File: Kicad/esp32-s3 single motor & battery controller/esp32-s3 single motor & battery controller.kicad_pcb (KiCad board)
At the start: 4 copper layers, 38.8 x 40.3 mm, 92 parts, among them J1 JST SH SM04B, J2 7 pin FPC 0.3mm, J3 Molex_PicoBlade_53048-0310 Ho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, Q3 PMOS,Si7157DP, Q4 PMOS, SW1 SW_Push, SW2 SW_Push, U1 AP2112K-3.3, U2 DRV8311HRRWR, U4 BQ25060, U5 ESP32-S3, U6 74HC595, Y1 40mhz, 10ppm

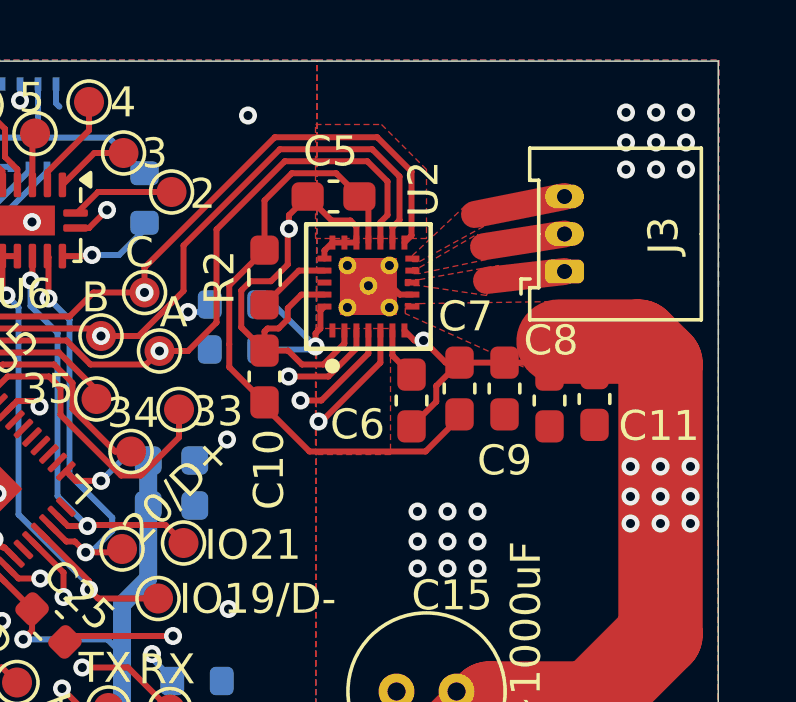
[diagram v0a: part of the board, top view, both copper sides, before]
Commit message: Started migrating driver to the back of the motor
If successful, this will save a ton of space. This will be a mess for awhile.
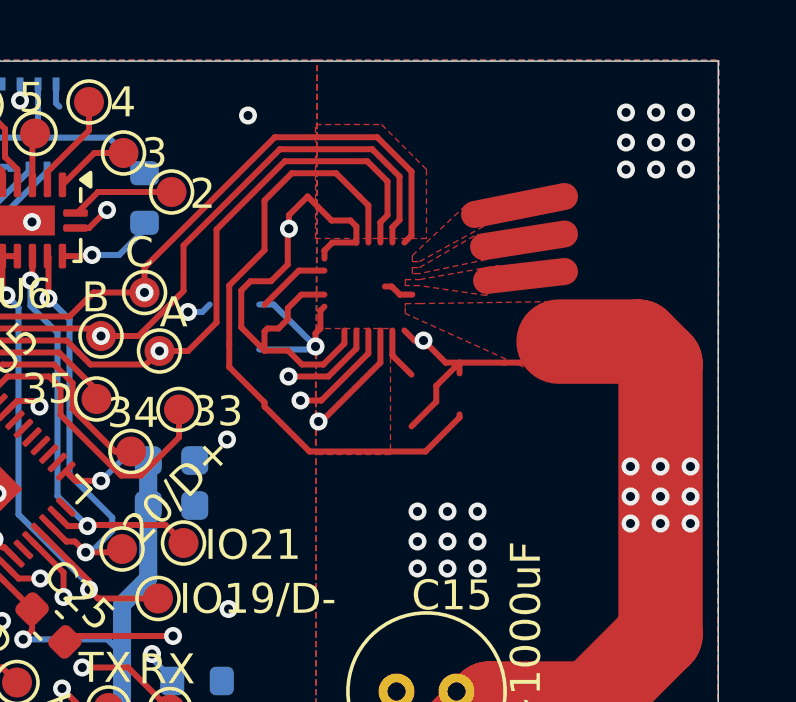
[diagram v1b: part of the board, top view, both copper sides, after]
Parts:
- removed C10: 0.1uF, Capacitor_SMD:C_0603_1608Metric_Pad1.08x0.95mm_HandSolder
- removed C11, C8: 22uF, Capacitor_SMD:C_0603_1608Metric_Pad1.08x0.95mm_HandSolder
- removed C5: 4.7uF, Capacitor_SMD:C_0603_1608Metric_Pad1.08x0.95mm_HandSolder
- removed C6, C7, C9: 0.1uF, 16v, Capacitor_SMD:C_0603_1608Metric_Pad1.08x0.95mm_HandSolder
- removed J3: Molex_PicoBlade_53048-0310 Horizontal 3P, Connector_Molex:Molex_PicoBlade_53048-0310_1x03_P1.25mm_Horizontal
- removed R1: 100k, Resistor_SMD:R_0603_1608Metric
- removed R2: 47k, Resistor_SMD:R_0603_1608Metric_Pad0.98x0.95mm_HandSolder
- removed R9: 150k, Resistor_SMD:R_0603_1608Metric
- removed U2: DRV8311HRRWR, custom_Driver_Motor:DRV8311_0.3mmVias
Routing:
- net (no net): track 0.00 -> 27.8 mm, vias 0 -> 2
- net /DRV8311/RegulatorOut: track 17.7 -> 0.00 mm, vias 1 -> 0
- net Net-(U2-SLEEP_N): track 5.82 -> 0.00 mm, vias 1 -> 0
- net Net-(U2-GAIN): track 2.47 -> 0.00 mm
- net Net-(U2-CP): track 1.74 -> 0.00 mm
- added copper zone on F.Cu, net (none)
- removed copper zone on F.Cu, net Net-(J3-Pin_1)
- removed copper zone on F.Cu, net Net-(J3-Pin_2)
- removed copper zone on F.Cu, net Net-(J3-Pin_3)

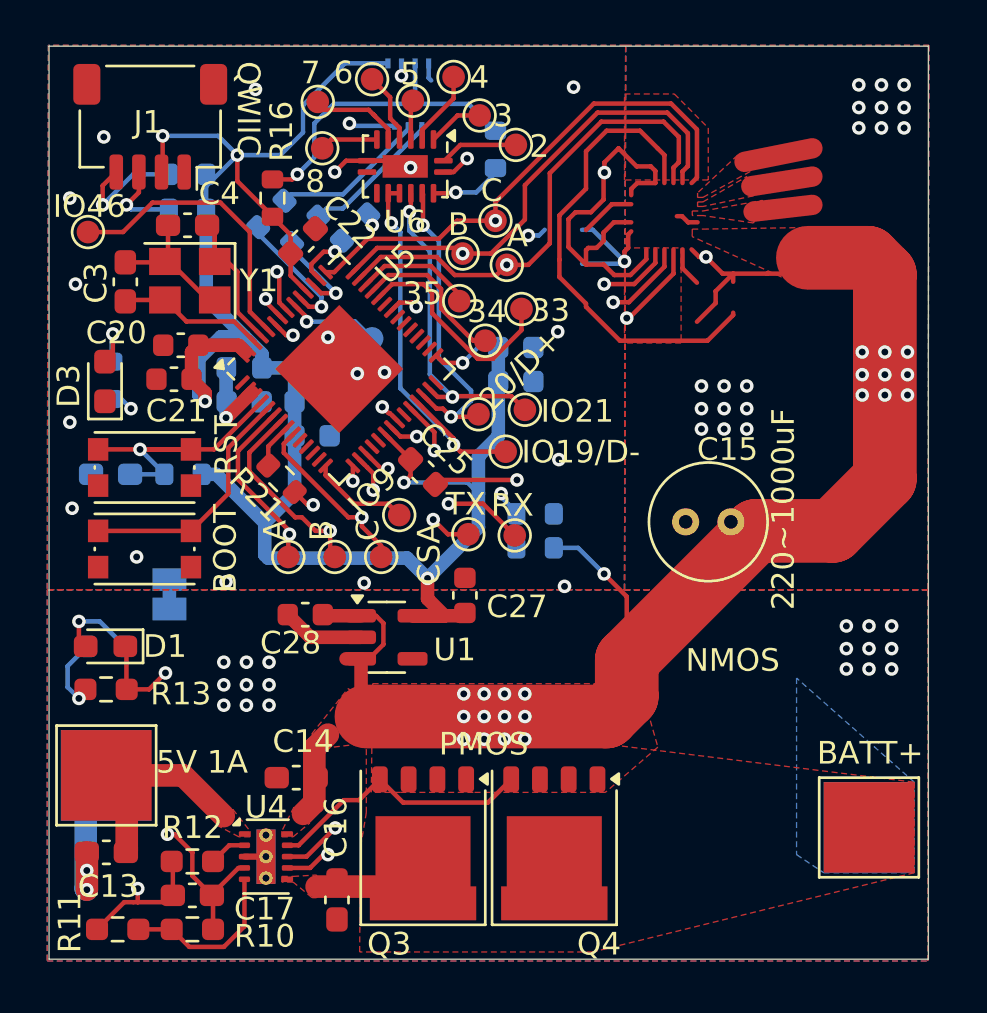
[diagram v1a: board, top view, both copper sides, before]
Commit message: Removed drv8311 section on the main board
Don't need it now that I have it off-board.
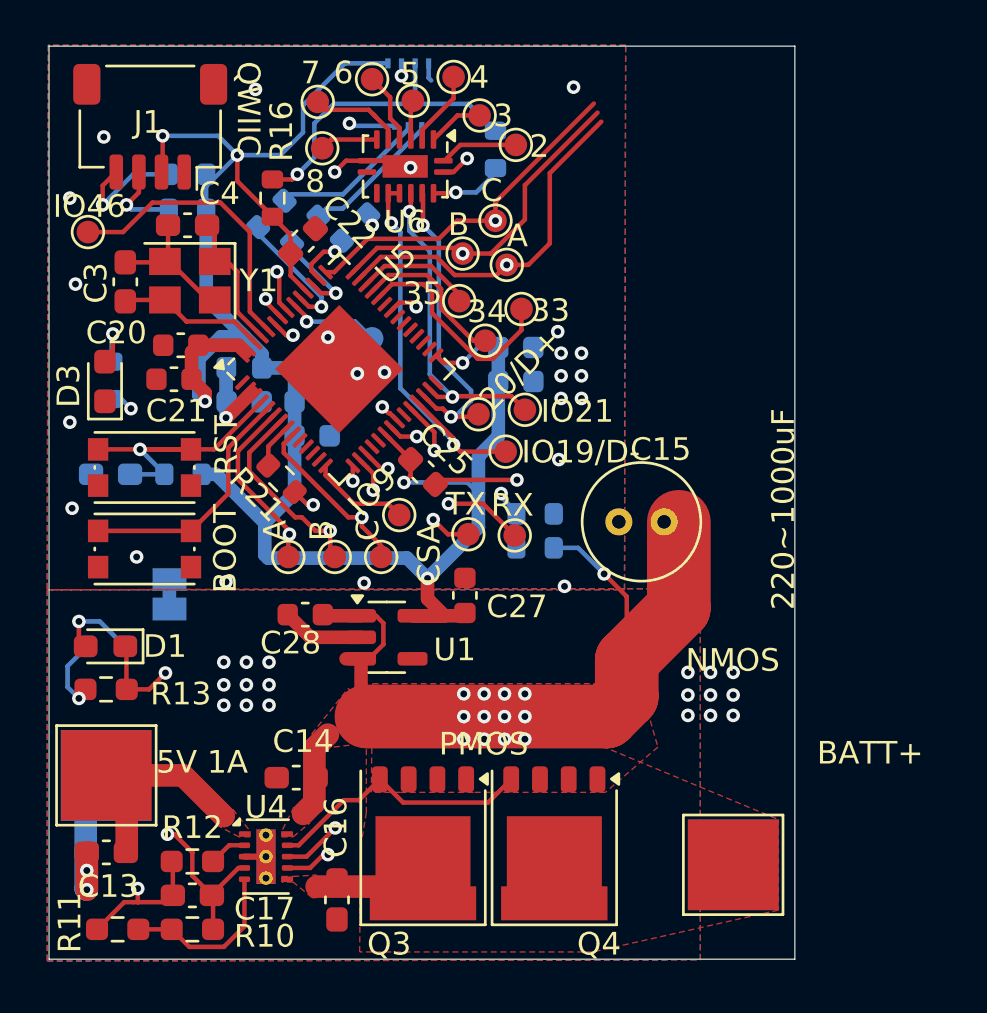
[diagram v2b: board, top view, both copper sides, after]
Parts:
- moved H1 6.22 mm to (152.9, 126.0)
- moved H2 6.22 mm to (152.9, 126.0)
- moved C15 2.95 mm to (149.8, 110.9)
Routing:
- net /MOTORPWR: track 114.5 -> 60.2 mm, vias 24 -> 13
- net (no net): track 27.8 -> 0.00 mm, vias 2 -> 0
- net GND: track 72.7 -> 51.6 mm
- net /1C: track 30.4 -> 22.9 mm
- net /1B: track 30.8 -> 24.2 mm
- net /1A: track 32.4 -> 26.6 mm
- net /1CSA-A: track 36.9 -> 33.0 mm, vias 2 -> 1
- net /1CSA-B: track 35.8 -> 32.1 mm, vias 2 -> 1
- net /1CSA-C: track 32.2 -> 28.9 mm, vias 2 -> 1
- net GNDPWR: track 12.7 -> 11.7 mm, vias 38 -> 26
- removed copper zone on F.Cu, net (none)
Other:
- board size 38.8 x 40.3 mm -> 32.9 x 40.3 mm

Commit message: Mostly finished Mainboard, adding silkscreen to magnetic encoder
I added pin headers to support my external driver board, and shrunk the whole design
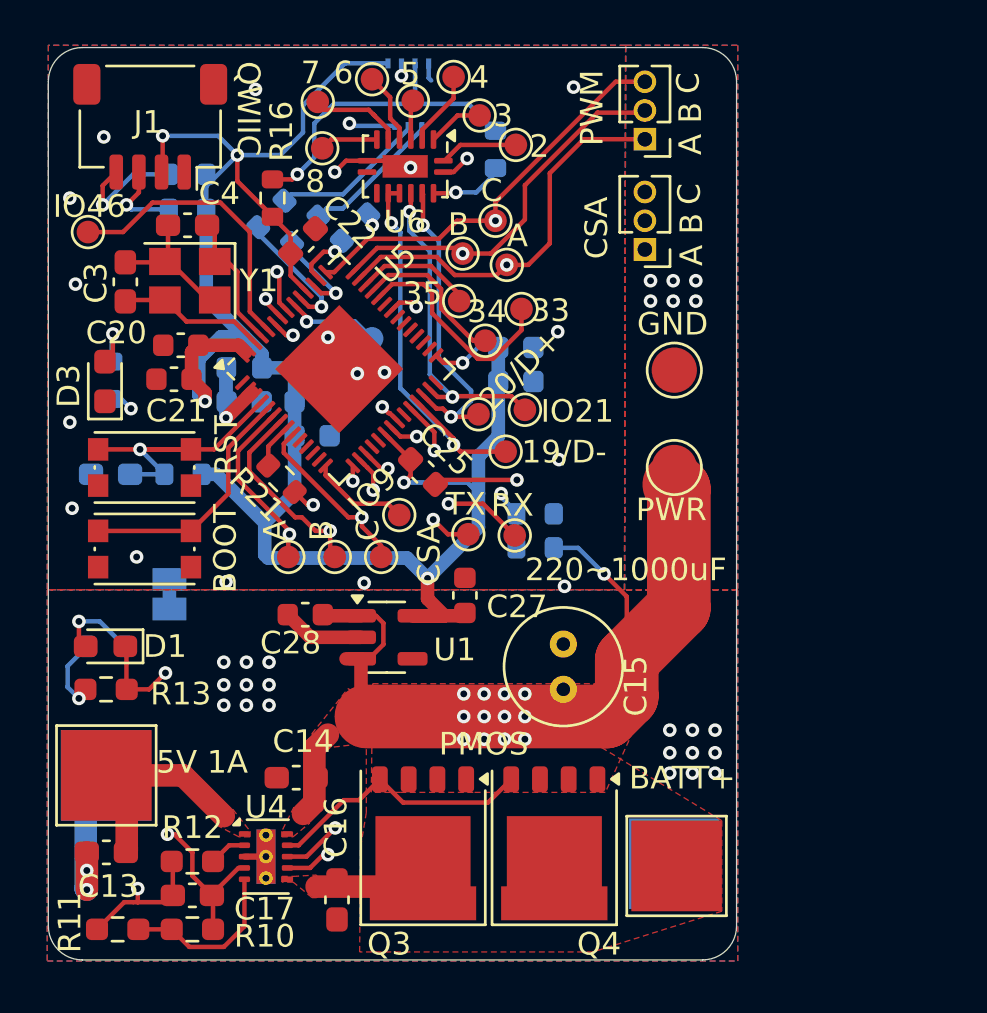
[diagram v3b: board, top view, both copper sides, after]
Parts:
- added H5: GND, TestPoint:TestPoint_Pad_D2.0mm, F.Cu at (150.3, 104.2)
- added H6: Power, TestPoint:TestPoint_Pad_D2.0mm, F.Cu at (150.3, 108.5)
- added J3: Conn_01x03, Connector_PinHeader_1.27mm:PinHeader_1x03_P1.27mm_Vertical, F.Cu at (149.0, 94.0)
- added J4: Conn_01x03, Connector_PinHeader_1.27mm:PinHeader_1x03_P1.27mm_Vertical, F.Cu at (149.0, 98.9)
- moved C15 8.63 mm to (145.4, 118.3), turned to 90 degrees
- moved H2 2.60 mm to (150.3, 126.0)
- moved H1 2.50 mm to (150.4, 126.1)
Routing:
- net /MOTORPWR: track 60.2 -> 41.5 mm
- net /1CSA-C: track 28.9 -> 33.3 mm
- net /1CSA-B: track 32.1 -> 35.7 mm
- net /1CSA-A: track 33.0 -> 36.1 mm
- net /1C: track 22.9 -> 25.6 mm
- net /1B: track 24.2 -> 26.3 mm
- net /1A: track 26.6 -> 28.2 mm
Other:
- board size 32.9 x 40.3 mm -> 30.4 x 40.3 mm
- board text added: "19/D-"
- board text added: "Encoder"
- board text added: "PWM"
- board text added: "PWR"
- board text added: "|||||||"
- board text added: "© 2024 Asher Edwards"
- board text removed: "Contacts facing PCB"
- board text removed: "Encoder FPC"
- board text removed: "IO19/D-"
- board text removed: "NMOS"
- board text removed: "© 2024 Asher James Edwards"

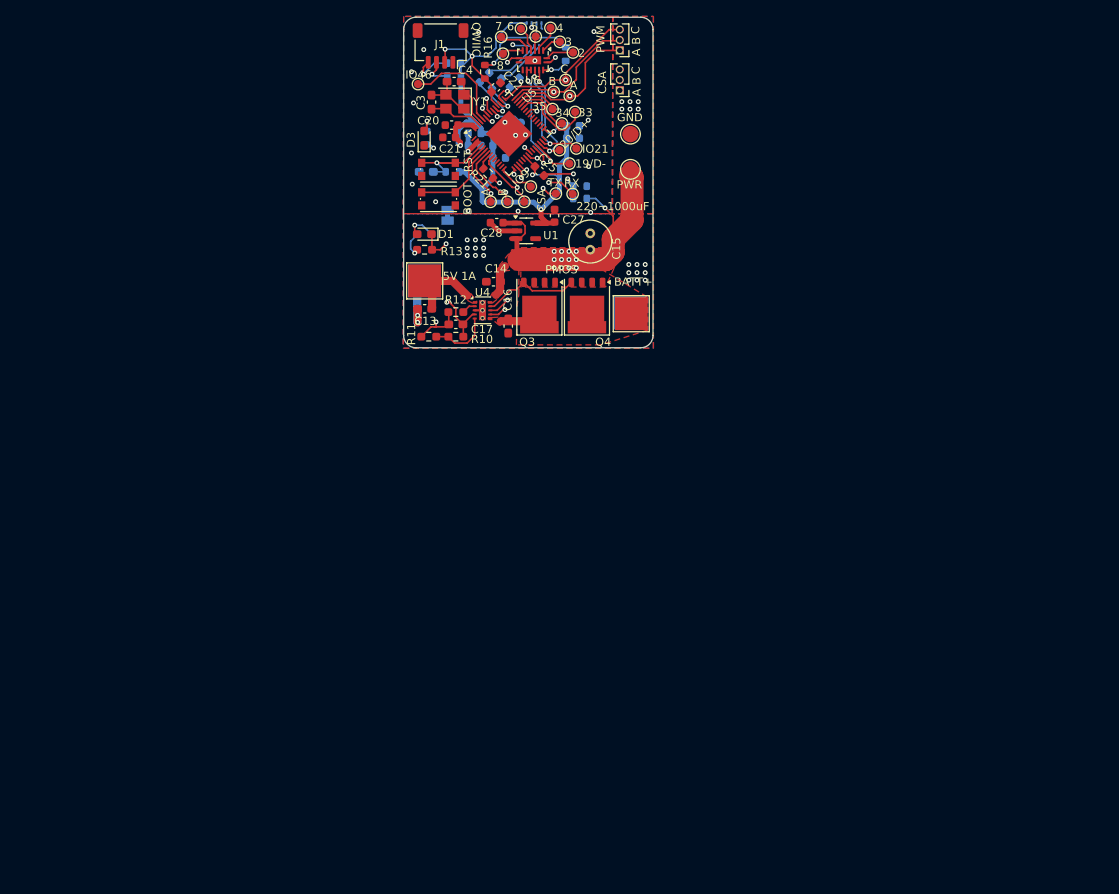
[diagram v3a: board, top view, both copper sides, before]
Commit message: Added footprints and started layout
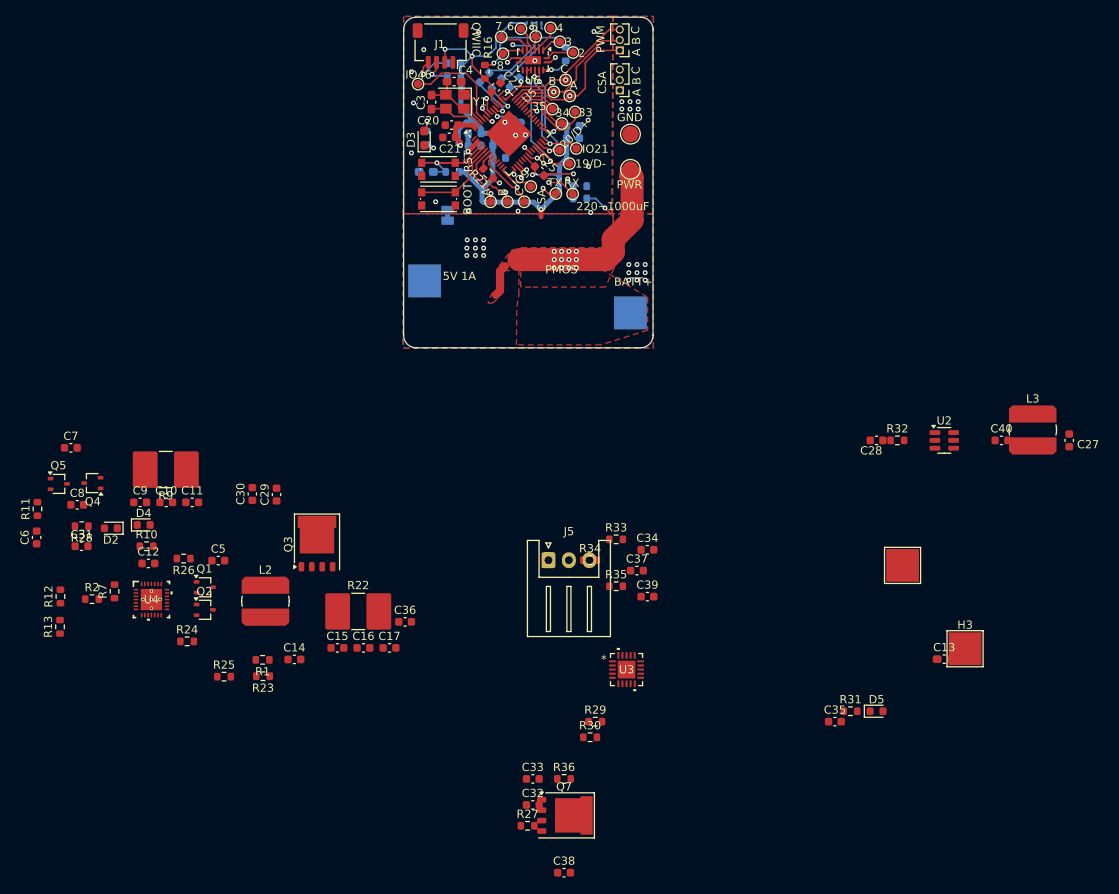
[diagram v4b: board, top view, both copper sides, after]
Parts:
- removed D1: Osram LT Q99G.01 green led, LED_SMD:LED_0603_1608Metric_Pad1.05x0.95mm_HandSolder
- removed R8: 402 ohm, Resistor_SMD:R_0603_1608Metric
- removed U1: AP2112K-3.3, Package_TO_SOT_SMD:SOT-23-5
- added C10: 0.1uF, Capacitor_SMD:C_0603_1608Metric, F.Cu at (93.7, 149.1)
- added C11: 0.01uF, Capacitor_SMD:C_0603_1608Metric, F.Cu at (96.9, 149.1)
- added C12: 1uf, Capacitor_SMD:C_0603_1608Metric, F.Cu at (91.5, 156.6)
- added C29: 10uF, Capacitor_SMD:C_0603_1608Metric, F.Cu at (107.2, 148.2)
- added C30: 10uF, Capacitor_SMD:C_0603_1608Metric, F.Cu at (104.2, 148.1)
- added C31: 2.2uf, Capacitor_SMD:C_0603_1608Metric, F.Cu at (83.4, 154.4)
- added C32: 100pF, Capacitor_SMD:C_0603_1608Metric, F.Cu at (138.4, 186.0)
- added C33: 0.1uF, Capacitor_SMD:C_0603_1608Metric, F.Cu at (138.4, 182.8)
- added C34: 22nF, Capacitor_SMD:C_0603_1608Metric, F.Cu at (152.4, 154.9)
- added C35: 2.2uf, Capacitor_SMD:C_0603_1608Metric, F.Cu at (175.2, 175.8)
- added C36: 10uF, Capacitor_SMD:C_0603_1608Metric, F.Cu at (122.8, 163.7)
- added C37: 220nF, Capacitor_SMD:C_0603_1608Metric, F.Cu at (151.1, 157.4)
- added C38: 0.1uF, Capacitor_SMD:C_0603_1608Metric, F.Cu at (142.2, 194.2)
- added C39: 220nF, Capacitor_SMD:C_0603_1608Metric, F.Cu at (152.4, 160.6)
- added C40: 100nF, Capacitor_SMD:C_0603_1608Metric, F.Cu at (195.5, 141.5)
- added C5: 47nF, Capacitor_SMD:C_0603_1608Metric, F.Cu at (100.0, 156.2)
- added C6: 2.2uf, Capacitor_SMD:C_0603_1608Metric, F.Cu at (77.9, 153.4)
- added C7: 1nF, Capacitor_SMD:C_0603_1608Metric, F.Cu at (82.1, 142.4)
- added C8: 47nf, Capacitor_SMD:C_0603_1608Metric, F.Cu at (82.8, 149.4)
- added C9: 0.1uF, Capacitor_SMD:C_0603_1608Metric, F.Cu at (90.5, 149.1)
- added D2: D, Diode_SMD:D_0603_1608Metric, F.Cu at (87.0, 152.2)
- added D4: D, Diode_SMD:D_0603_1608Metric, F.Cu at (91.0, 151.8)
- added D5: D, Diode_SMD:D_0603_1608Metric, F.Cu at (180.3, 174.6)
- added J5: Batt Balance connector, Connector_JST:JST_XH_S3B-XH-A_1x03_P2.50mm_Horizontal, F.Cu at (140.3, 156.2)
- added L2: 5.6uH, 2.2A < sat, Inductor_SMD:L_Bourns_SDR0604, F.Cu at (105.8, 161.2)
- added L3: 4.7uH, Inductor_SMD:L_Bourns_SDR0604, F.Cu at (199.3, 140.3)
- added Q1: NMOS,12v, Package_TO_SOT_SMD:SOT-323_SC-70, F.Cu at (98.4, 159.4)
- added Q2: NMOS, 12v, Package_TO_SOT_SMD:SOT-323_SC-70, F.Cu at (98.4, 162.2)
- added Q5: NMOS, 12v, Package_TO_SOT_SMD:SOT-323_SC-70, F.Cu at (80.6, 146.8)
- added Q7: NMOS,12v,PPak, Package_DFN_QFN:PQFN-8-EP_6x5mm_P1.27mm_Generic, F.Cu at (142.2, 187.3)
- added R1: 10ohm, Resistor_SMD:R_0603_1608Metric, F.Cu at (105.5, 168.3)
- added R2: 4.02k, Resistor_SMD:R_0603_1608Metric, F.Cu at (84.7, 160.9)
- added R22: 10mOhm, CS, Resistor_SMD:R_2816_7142Metric, F.Cu at (117.1, 162.4)
- added R23: 10ohm, Resistor_SMD:R_0603_1608Metric, F.Cu at (105.5, 170.3)
- added R24: 10ohm, Resistor_SMD:R_0603_1608Metric, F.Cu at (96.2, 166.1)
- added R25: 4.02kohm, Resistor_SMD:R_0603_1608Metric, F.Cu at (100.8, 170.3)
- added R26: 100k, Resistor_SMD:R_0603_1608Metric, F.Cu at (95.8, 155.9)
- added R27: 10mOhm, Resistor_SMD:R_0603_1608Metric, F.Cu at (137.8, 188.5)
- added R28: 2ohm, Resistor_SMD:R_0603_1608Metric, F.Cu at (83.4, 152.0)
- added R29: 100ohm, Resistor_SMD:R_0603_1608Metric, F.Cu at (146.0, 175.8)
- added R30: 100ohm, Resistor_SMD:R_0603_1608Metric, F.Cu at (145.4, 177.7)
- added R31: 10k, Resistor_SMD:R_0603_1608Metric, F.Cu at (177.1, 174.6)
- added R32: 10k, Resistor_SMD:R_0603_1608Metric, F.Cu at (182.8, 141.5)
- added R33: 10ohm, Resistor_SMD:R_0603_1608Metric, F.Cu at (148.6, 153.6)
- added R34: 10ohm, Resistor_SMD:R_0603_1608Metric, F.Cu at (145.4, 156.2)
- added R35: 10ohm, Resistor_SMD:R_0603_1608Metric, F.Cu at (148.6, 159.3)
- added R36: 5.1k, Resistor_SMD:R_0603_1608Metric, F.Cu at (142.2, 182.8)
- added R7: 4.02k, Resistor_SMD:R_0603_1608Metric, F.Cu at (87.4, 159.9)
- added R9: 10mOhm CS, Resistor_SMD:R_2816_7142Metric, F.Cu at (93.7, 145.1)
- added U2: AP63203WU, Package_TO_SOT_SMD:TSOT-23-6, F.Cu at (188.6, 141.5)
- added U3: BQ76905RGRR, BQ76905:VQFN20_RGR_TEX, F.Cu at (149.8, 169.5)
- C14: value 10uF, 16v -> 2.2uf; footprint Capacitor_SMD:C_0603_1608Metric_Pad1.08x0.95mm_HandSolder -> Capacitor_SMD:C_0603_1608Metric
- C15: value 1000uF, 16v -> 0.1uF; footprint Capacitor_THT:C_Radial_D5.0mm_H5.0mm_P2.00mm -> Capacitor_SMD:C_0603_1608Metric
- C16: value 10uF, 16v -> 0.1uF; footprint Capacitor_SMD:C_0603_1608Metric_Pad1.08x0.95mm_HandSolder -> Capacitor_SMD:C_0603_1608Metric
- C17: value 1uF -> 0.1uF; footprint Capacitor_SMD:C_0603_1608Metric_Pad1.08x0.95mm_HandSolder -> Capacitor_SMD:C_0603_1608Metric
- Q3: value PMOS,Si7157DP -> NMOS,12v,PPak
- Q4: value PMOS -> NMOS, 12v; footprint Package_DFN_QFN:PQFN-8-EP_6x5mm_P1.27mm_Generic -> Package_TO_SOT_SMD:SOT-323_SC-70
- R10: value 1k -> 10k; footprint Resistor_SMD:R_0603_1608Metric_Pad0.98x0.95mm_HandSolder -> Resistor_SMD:R_0603_1608Metric
- R11: value 230ohm -> 2ohm; footprint Resistor_SMD:R_0603_1608Metric_Pad0.98x0.95mm_HandSolder -> Resistor_SMD:R_0603_1608Metric
- R12: value 1k -> 866k; footprint Resistor_SMD:R_0603_1608Metric_Pad0.98x0.95mm_HandSolder -> Resistor_SMD:R_0603_1608Metric
- R13: value 2k -> 133k; footprint Resistor_SMD:R_0603_1608Metric_Pad0.98x0.95mm_HandSolder -> Resistor_SMD:R_0603_1608Metric
- U4: value BQ25060 -> BQ24780SRUYR; footprint custom_Power:WSON-10-1EP_2x3mm_P0.5mm_EP0.84x2.4mm_ThermalVias_0.3mm -> BQ24780:RUY0028A
- moved H3 79.7 mm to (191.1, 166.9)
- moved C13 76.4 mm to (188.6, 168.2), turned to 0 degrees
- moved C27 68.5 mm to (203.8, 141.5)
- moved Q4 64.1 mm to (84.7, 146.8), turned to 180 degrees
- moved R13 63.9 mm to (80.8, 164.3), turned to 90 degrees
- moved R12 59.4 mm to (80.8, 160.6), turned to 90 degrees
- moved C15 57.5 mm to (114.6, 166.8), turned to 0 degrees
- moved U4 53.6 mm to (91.9, 160.9)
- moved C28 53.4 mm to (180.3, 141.5)
- moved R11 52.1 mm to (78.0, 149.9), turned to 90 degrees
- moved C14 52.1 mm to (109.3, 168.2), turned to 0 degrees
- moved R10 45.6 mm to (91.3, 154.4), turned to 0 degrees
- moved H1 45.1 mm to (183.5, 156.8)
- moved C16 43.0 mm to (117.7, 166.8), turned to 0 degrees
- moved C17 40.3 mm to (120.9, 166.8)
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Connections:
- C14 pad 1: /MOTORPWR -> /PSU/REGN
- C15 pad 1: /MOTORPWR -> GNDPWR
- C15 pad 2: GNDPWR -> Net-(Q3-S)
- C16 pad 1: GNDPWR -> Net-(Q3-S)
- C17 pad 1: GND -> /PSU/BATT+
- C17 pad 2: /PSU/LDO 4.9v -> GNDPWR
- H2 pad 1: GNDPWR -> /PSU/BATT-
- Q3 pad 5: /PSU/BATT+ -> Net-(Q3-S)
- Q4 pad 1: /MOTORPWR -> Net-(Q4-D)
- Q4 pad 2: /MOTORPWR -> Net-(Q4-G)
- Q4 pad 3: /MOTORPWR -> Net-(Q4-S)
- R10 pad 1: /PSU/LDO 4.9v -> Net-(U4-VCC)
- R10 pad 2: Net-(U4-TS) -> Net-(D2-K)
- R11 pad 1: Net-(U4-TS) -> Net-(C6-Pad1)
- R11 pad 2: GND -> /PSU/IN
- R12 pad 1: GND -> Net-(U4-ACDET)
- R12 pad 2: Net-(U4-ISET) -> /PSU/IN
- R13 pad 1: /PSU/~{CHG} -> GNDPWR
- R13 pad 2: /PSU/LDO 4.9v -> Net-(U4-ACDET)
- U4 pad 1: /PSU/IN -> /MOTORPWR
- U4 pad 10: /MOTORPWR -> unconnected-(U4-PROCHOT_N-Pad10)
- U4 pad 11: GNDPWR -> /SDA1
- U4 pad 2: Net-(U4-ISET) -> Net-(Q4-D)
- U4 pad 3: GNDPWR -> Net-(U4-CMSRC)
- U4 pad 4: /PSU/LDO 4.9v -> Net-(U4-ACDRV)
- U4 pad 5: Net-(U4-TS) -> unconnected-(U4-ACOK-Pad5)
- U4 pad 6: /PSU/BATT+ -> Net-(U4-ACDET)
- U4 pad 7: GND -> unconnected-(U4-IADP-Pad7)
- U4 pad 8: /PSU/~{CHG} -> unconnected-(U4-IDCHG-Pad8)
- U4 pad 9: Net-(Q3-G) -> unconnected-(U4-PMON-Pad9)
- U6 pad 17: GND -> (no net)
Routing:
- net GND: track 51.6 -> 15.8 mm, vias 23 -> 20
- net /PSU/LDO 4.9v: track 28.3 -> 0.00 mm, vias 2 -> 0
- net /PSU/~{CHG}: track 17.9 -> 0.00 mm, vias 2 -> 0
- net Net-(Q3-G): track 11.9 -> 0.00 mm
- net GNDPWR: track 11.7 -> 1.27 mm, vias 26 -> 24
- net /PSU/IN: track 9.64 -> 0.00 mm
- net /MOTORPWR: track 41.5 -> 33.5 mm
- net Net-(U4-TS): track 7.46 -> 0.00 mm
- net VDD: track 103.8 -> 98.9 mm
- net Net-(D1-A): track 3.70 -> 0.00 mm, vias 1 -> 0
- net /PSU/BATT+: track 2.69 -> 0.00 mm
- net Net-(U4-ISET): track 1.68 -> 0.00 mm
- removed copper zone on F.Cu, net /PSU/IN
